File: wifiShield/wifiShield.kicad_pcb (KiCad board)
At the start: 2 copper layers, 32.3 x 40.6 mm, 21 parts, among them J1 USB_OTG, J2 CONN_02X06, J3 CONN_01X13, J4 CONN_01X05, J7 CONN_01X08, SW1 SW_Push, SW2 SW_Push, U2 FT232RL, U3 esp8266mod

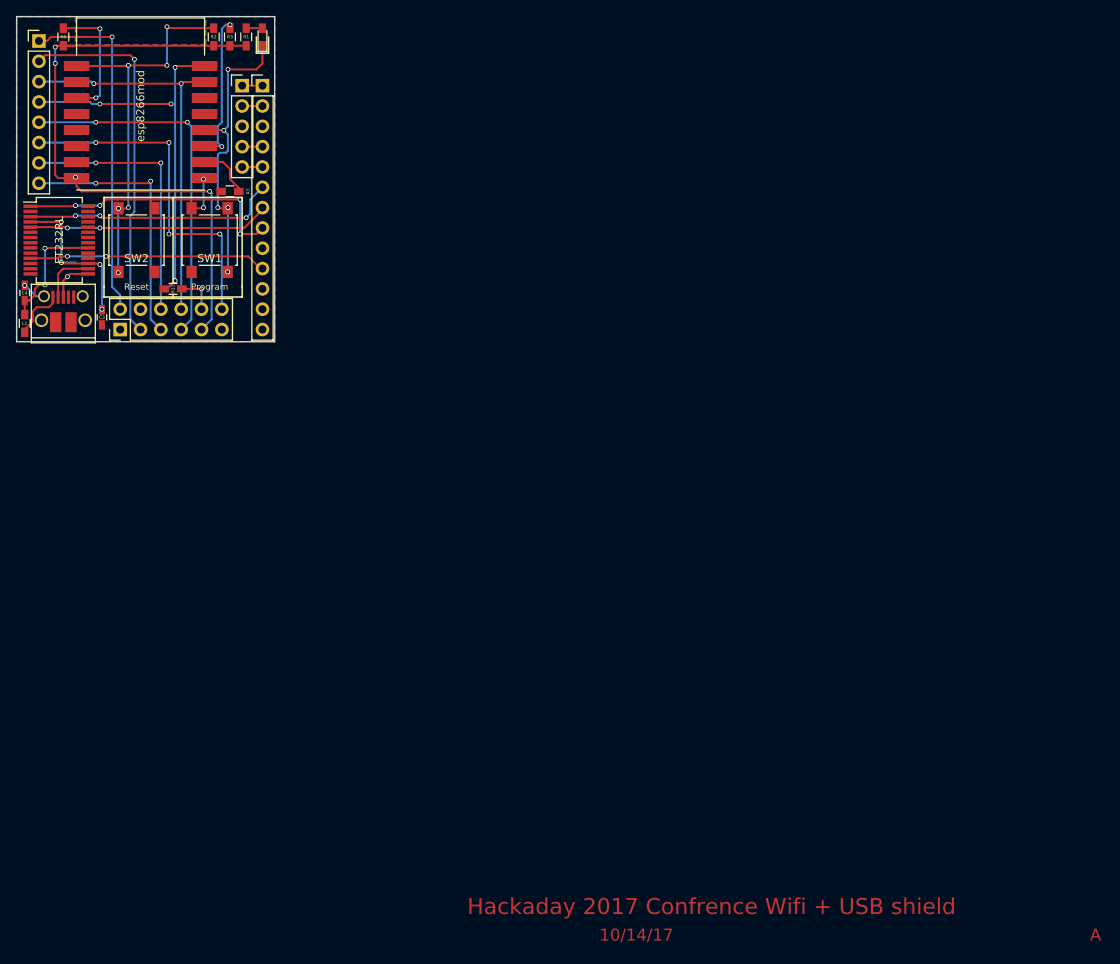
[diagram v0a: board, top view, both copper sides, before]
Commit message: Remove extra via and add REV to board
Board Rev bumped to Rev B
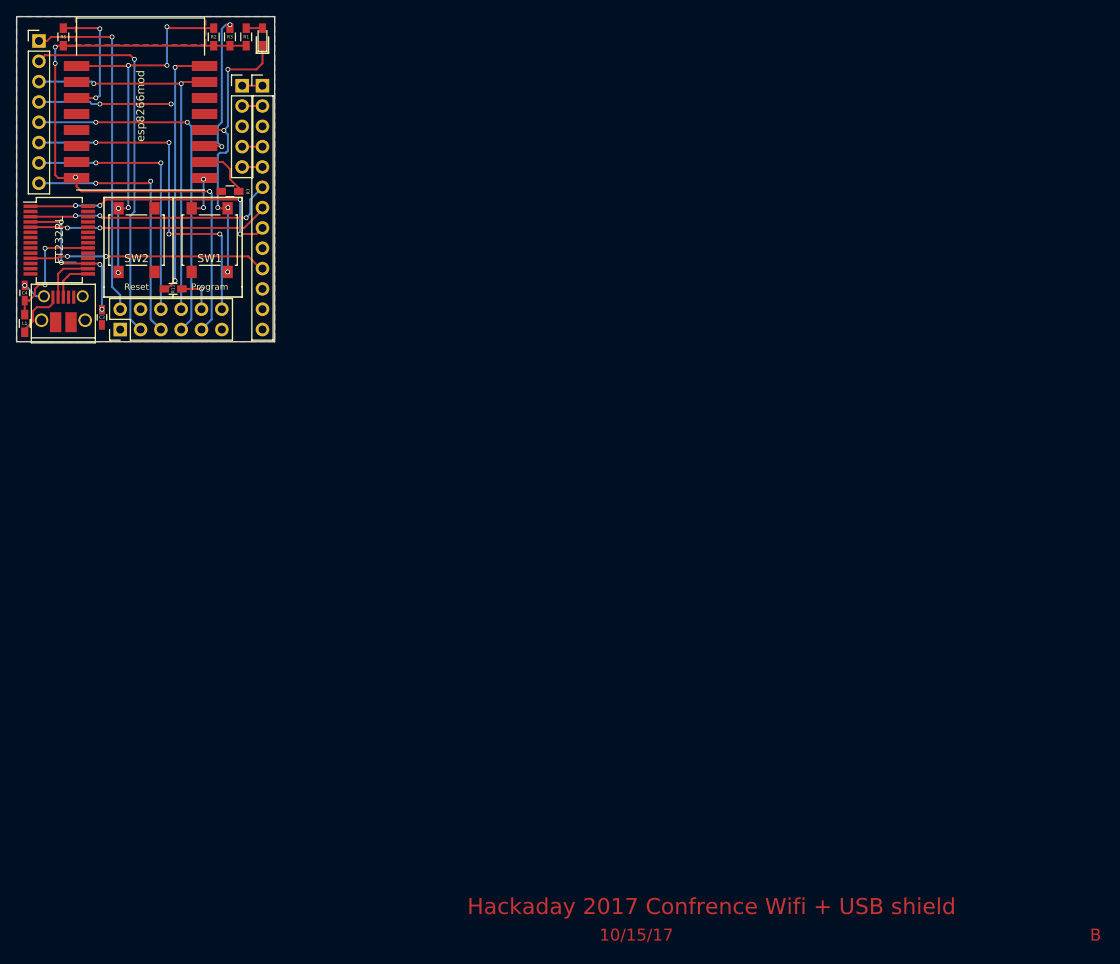
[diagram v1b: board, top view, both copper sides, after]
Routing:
- net Net-(J1-Pad3): vias 1 -> 0
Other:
- board text added: "10/15/17"
- board text added: "B"
- board text added: "REV: B"
- board text removed: "10/14/17"
- board text removed: "A"
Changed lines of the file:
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@@
     (links 64)
     (no_connects 0)
-    (area 132.126667 77.975 174.55762 122.053)
+    (area 132.126667 77.975 269.882857 194.39)
     (thickness 1.6)
-    (drawings 67)
-    (tracks 259)
+    (drawings 69)
+    (tracks 258)
     (zones 0)
     (modules 21)
@@
       (net 1 GND))
   )
-  (gr_text A (at 269.24 193.04) (layer F.Cu)
+  (gr_text "REV: B" (at 161.544 112.014) (layer B.SilkS)
+    (effects (font (size 0.5 0.5) (thickness 0.1)) (justify mirror))
+  )
+  (gr_text "REV: B" (at 130.048 106.426) (layer B.SilkS)
+    (effects (font (size 0.5 0.5) (thickness 0.1)) (justify mirror))
+  )
+  (gr_text B (at 269.24 193.04) (layer F.Cu)
     (effects (font (size 1.5 1.5) (thickness 0.3)))
   )
-  (gr_text "10/14/17\n" (at 211.836 193.04) (layer F.Cu)
+  (gr_text "10/15/17\n" (at 211.836 193.04) (layer F.Cu)
     (effects (font (size 1.5 1.5) (thickness 0.3)))
   )
@@
     (effects (font (size 0.8 0.8) (thickness 0.15)))
   )
-  (gr_text 10/14/17 (at 160.782 112.776) (layer B.SilkS)
+  (gr_text 10/15/17 (at 160.782 112.776) (layer B.SilkS)
     (effects (font (size 0.5 0.5) (thickness 0.1)) (justify mirror))
   )
@@
   (segment (start 139.558 110.378) (end 140.189 109.747) (width 0.25) (layer F.Cu) (net 29))
   (segment (start 140.208 113.308) (end 140.208 111.252) (width 0.25) (layer F.Cu) (net 30))
-  (via (at 140.716 110.744) (size 0.6) (drill 0.4) (layers F.Cu B.Cu) (net 30))
   (segment (start 140.716 110.744) (end 141.063 110.397) (width 0.25) (layer F.Cu) (net 30))
   (segment (start 141.063 110.397) (end 143.3 110.397) (width 0.25) (layer F.Cu) (net 30))
